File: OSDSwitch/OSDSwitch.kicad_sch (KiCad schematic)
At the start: 15 parts, among them IC1 ADG1633BCPZ-REEL7, J1 Conn_01x03_Pin, J2 Conn_01x03_Pin, J3 Conn_01x03_Pin, J4 Conn_01x05, J5 Conn_01x04, J6 Conn_01x02

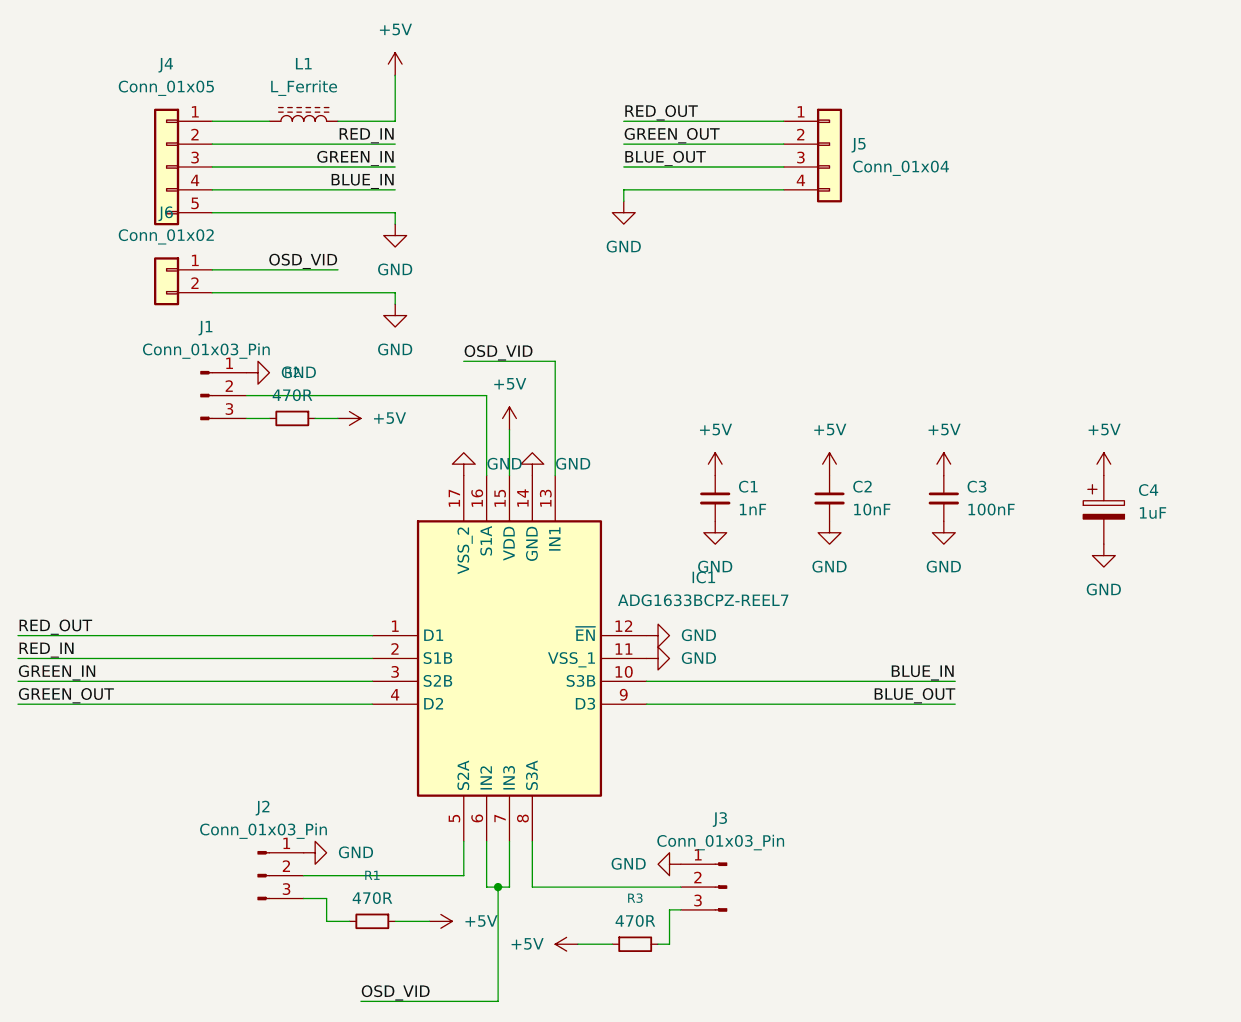
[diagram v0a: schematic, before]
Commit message: Corrected chip footprint
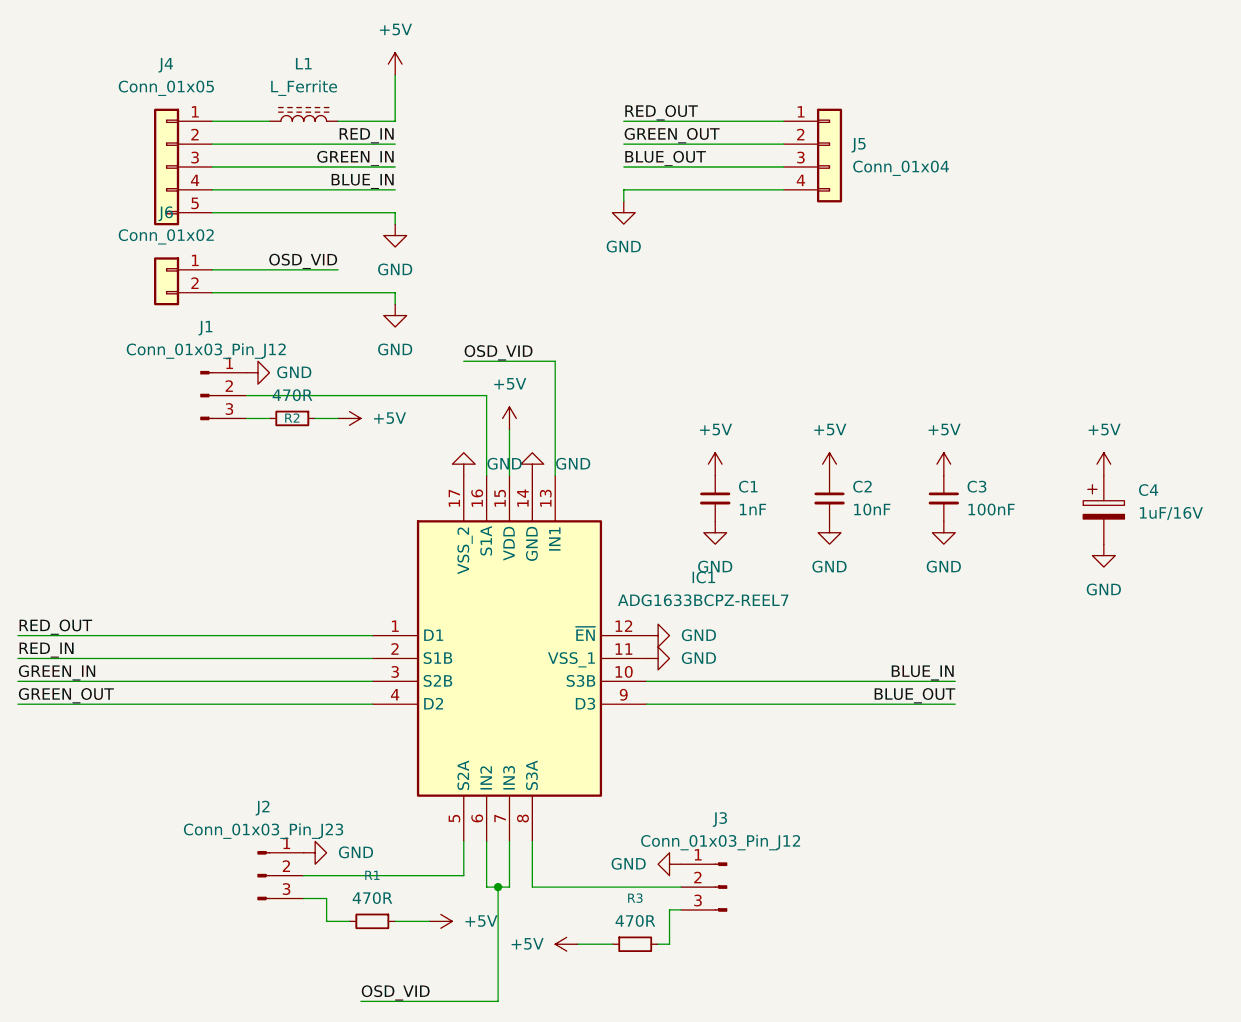
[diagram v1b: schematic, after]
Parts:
- C4: value 1uF -> 1uF/16V
- IC1: footprint Package_DFN_QFN:QFN-16-1EP_4x4mm_P0.5mm_EP2.45x2.45mm -> Package_DFN_QFN:QFN-16-1EP_3x3mm_P0.5mm_EP1.75x1.75mm
- J1, J3: value Conn_01x03_Pin -> Conn_01x03_Pin_J12
- J2: value Conn_01x03_Pin -> Conn_01x03_Pin_J23
- R1, R2, R3: footprint Capacitor_SMD:C_0402_1005Metric -> Resistor_SMD:R_0402_1005Metric
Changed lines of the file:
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@@
 		(on_board yes)
 		(dnp no)
-		(fields_autoplaced yes)
 		(property "Reference" "#PWR04"
 			(at 82.55 53.34 0)
@@
 		)
 		(property "Value" "GND"
-			(at 80.01 53.3399 90)
+			(at 79.502 53.34 90)
 			(effects
 				(font
@@
 			)
 		)
-		(property "Value" "1uF"
+		(property "Value" "1uF/16V"
 			(at 175.26 68.9609 0)
 			(effects
@@
 			)
 		)
-		(property "Value" "Conn_01x03_Pin"
+		(property "Value" "Conn_01x03_Pin_J12"
 			(at 128.905 105.41 0)
 			(effects
@@
 			)
 		)
-		(property "Value" "Conn_01x03_Pin"
+		(property "Value" "Conn_01x03_Pin_J23"
 			(at 78.105 104.14 0)
 			(effects
@@
 			)
 		)
-		(property "Footprint" "Capacitor_SMD:C_0402_1005Metric"
+		(property "Footprint" "Resistor_SMD:R_0402_1005Metric"
 			(at 119.38 116.84 0)
 			(effects
@@
 			)
 		)
-		(property "Value" "Conn_01x03_Pin"
+		(property "Value" "Conn_01x03_Pin_J12"
 			(at 71.755 50.8 0)
 			(effects
@@
 			)
 		)
-		(property "Footprint" "Capacitor_SMD:C_0402_1005Metric"
+		(property "Footprint" "Resistor_SMD:R_0402_1005Metric"
 			(at 90.17 114.3 0)
 			(effects
@@
 			)
 		)
-		(property "Footprint" "Package_DFN_QFN:QFN-16-1EP_4x4mm_P0.5mm_EP2.45x2.45mm"
+		(property "Footprint" "Package_DFN_QFN:QFN-16-1EP_3x3mm_P0.5mm_EP1.75x1.75mm"
 			(at 116.84 167.31 0)
 			(effects
@@
 		(on_board yes)
 		(dnp no)
-		(fields_autoplaced yes)
 		(property "Reference" "R2"
-			(at 81.28 53.34 90)
+			(at 81.28 58.42 90)
 			(effects
 				(font
@@
 			)
 		)
-		(property "Footprint" "Capacitor_SMD:C_0402_1005Metric"
+		(property "Footprint" "Resistor_SMD:R_0402_1005Metric"
 			(at 81.28 58.42 0)
 			(effects

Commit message: Swapped red and blue to match Amiga 500 video output order
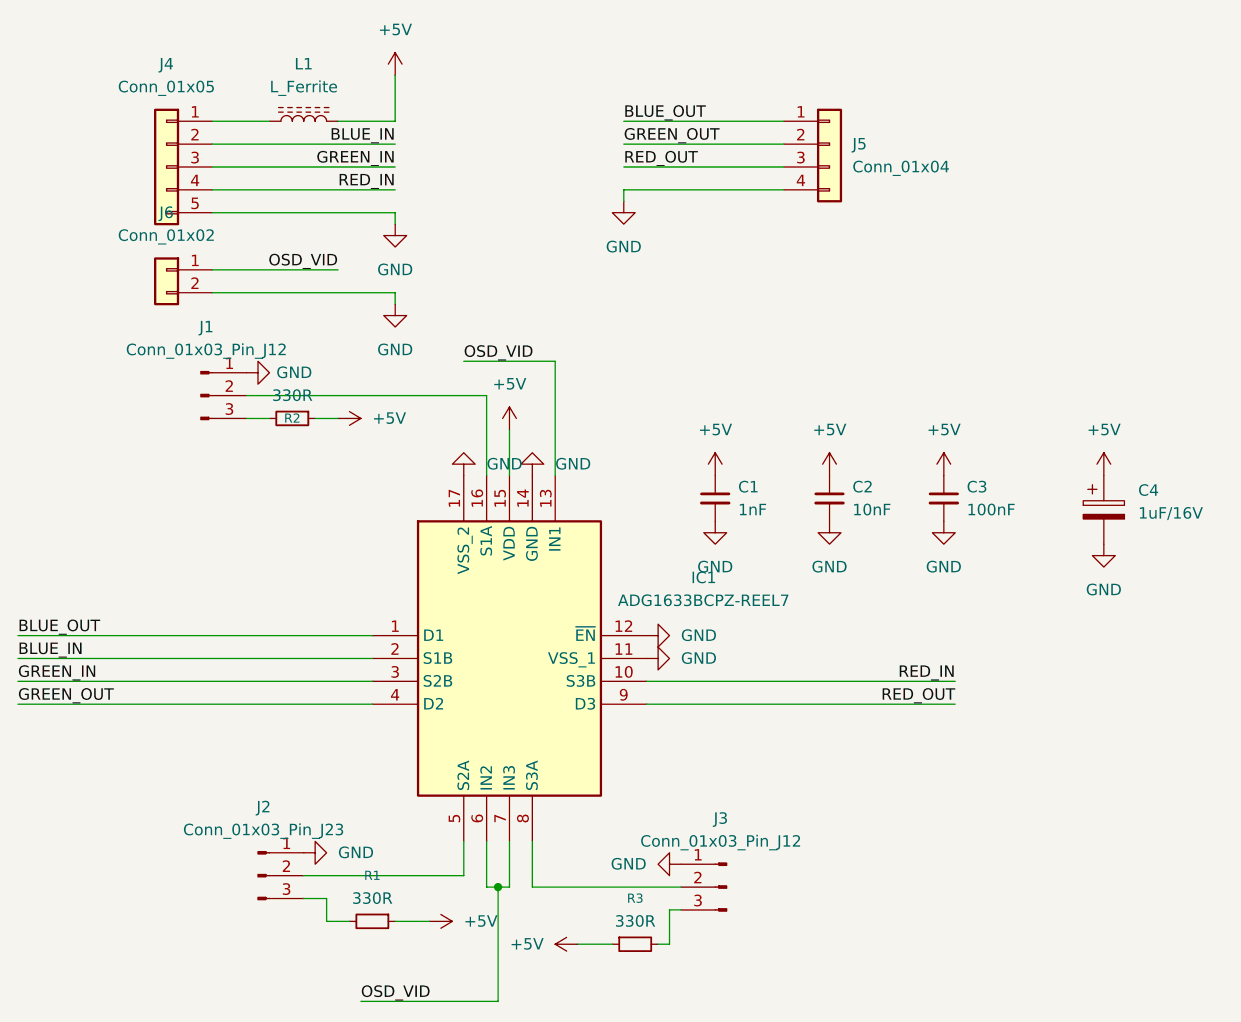
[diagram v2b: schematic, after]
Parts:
- R1, R2, R3: value 470R -> 330R
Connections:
- net BLUE_IN: now also IC1.2 (S1B), J4.2 (Pin_2); no longer IC1.10 (S3B), J4.4 (Pin_4)
- net BLUE_OUT: now also IC1.1 (D1), J5.1 (Pin_1); no longer IC1.9 (D3), J5.3 (Pin_3)
- net RED_IN: now also IC1.10 (S3B), J4.4 (Pin_4); no longer IC1.2 (S1B), J4.2 (Pin_2)
- net RED_OUT: now also IC1.9 (D3), J5.3 (Pin_3); no longer IC1.1 (D1), J5.1 (Pin_1)
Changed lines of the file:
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@@
 	)
 	(label "RED_IN"
-		(at 92.71 27.94 180)
+		(at 92.71 33.02 180)
 		(effects
 			(font
@@
 	)
 	(label "RED_OUT"
-		(at 118.11 25.4 0)
+		(at 118.11 30.48 0)
 		(effects
 			(font
@@
 	)
 	(label "BLUE_IN"
-		(at 92.71 33.02 180)
+		(at 92.71 27.94 180)
 		(effects
 			(font
@@
 	)
 	(label "RED_IN"
-		(at 50.8 85.09 0)
+		(at 154.94 87.63 180)
 		(effects
 			(font
 				(size 1.27 1.27)
 			)
-			(justify left bottom)
+			(justify right bottom)
 		)
 	)
 	(label "RED_OUT"
-		(at 50.8 82.55 0)
+		(at 154.94 90.17 180)
 		(effects
 			(font
 				(size 1.27 1.27)
 			)
-			(justify left bottom)
+			(justify right bottom)
 		)
 	)
@@
 	)
 	(label "BLUE_OUT"
-		(at 118.11 30.48 0)
+		(at 118.11 25.4 0)
 		(effects
 			(font
@@
 	)
 	(label "BLUE_IN"
-		(at 154.94 87.63 180)
+		(at 50.8 85.09 0)
 		(effects
 			(font
 				(size 1.27 1.27)
 			)
-			(justify right bottom)
+			(justify left bottom)
 		)
 	)
 	(label "BLUE_OUT"
-		(at 154.94 90.17 180)
+		(at 50.8 82.55 0)
 		(effects
 			(font
 				(size 1.27 1.27)
 			)
-			(justify right bottom)
+			(justify left bottom)
 		)
 	)
@@
 			)
 		)
-		(property "Value" "470R"
+		(property "Value" "330R"
 			(at 119.38 114.3 90)
 			(effects
@@
 			)
 		)
-		(property "Value" "470R"
+		(property "Value" "330R"
 			(at 90.17 111.76 90)
 			(effects
@@
 			)
 		)
-		(property "Value" "470R"
+		(property "Value" "330R"
 			(at 81.28 55.88 90)
 			(effects
